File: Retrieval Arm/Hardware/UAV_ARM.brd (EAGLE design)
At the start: 100 x 80 mm, 20 parts, among them Q1 Q_ATMEGA328P, Q2 Q_LTC490, Q3 Q_LDO, X1 X_HC49SCRYSTAL

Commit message: Revised Board #4
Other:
- board size 100 x 80 mm -> 54.6 x 47 mm
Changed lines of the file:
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@@
 <setting verticaltext="up"/>
 </settings>
-<grid distance="0.05" unitdist="inch" unit="inch" style="lines" multiple="1" display="no" altdistance="0.025" altunitdist="inch" altunit="inch"/>
+<grid distance="0.05" unitdist="inch" unit="inch" style="lines" multiple="1" display="yes" altdistance="0.005" altunitdist="inch" altunit="inch"/>
 <layers>
 <layer number="1" name="Top" color="4" fill="1" visible="yes" active="yes"/>
@@
 <board>
 <plain>
-<wire x1="0" y1="0" x2="100" y2="0" width="0" layer="20"/>
-<wire x1="100" y1="0" x2="100" y2="80" width="0" layer="20"/>
-<wire x1="100" y1="80" x2="0" y2="80" width="0" layer="20"/>
-<wire x1="0" y1="80" x2="0" y2="0" width="0" layer="20"/>
-<hole x="3.81" y="34.29" drill="0.6"/>
-<hole x="53.34" y="34.29" drill="0.6"/>
-<hole x="53.34" y="77.47" drill="0.6"/>
-<hole x="20.32" y="77.47" drill="0.6"/>
+<wire x1="0" y1="80.01" x2="0" y2="33.02" width="0" layer="20"/>
+<wire x1="0" y1="33.02" x2="54.61" y2="33.02" width="0" layer="20"/>
+<wire x1="54.61" y1="33.02" x2="54.61" y2="80.01" width="0" layer="20"/>
+<wire x1="54.61" y1="80.01" x2="0" y2="80.01" width="0" layer="20"/>
 </plain>
 <attributes>

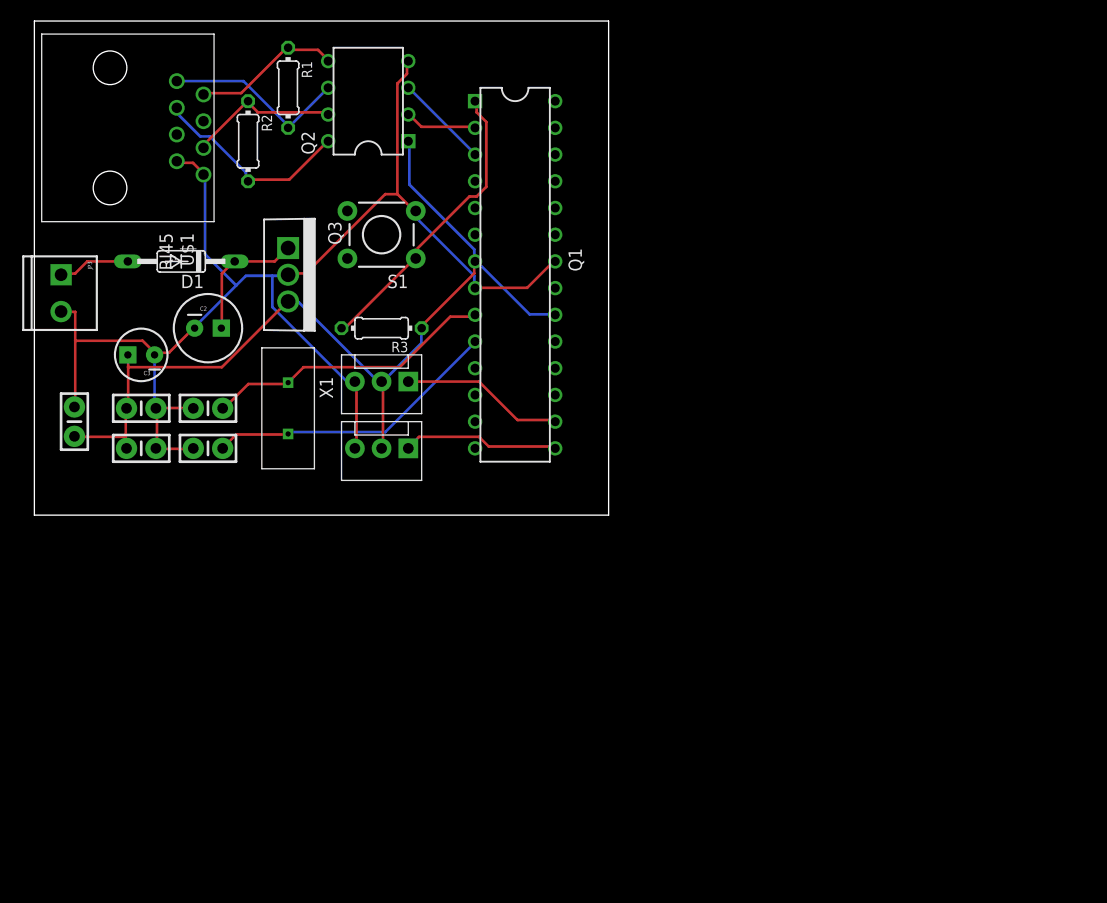
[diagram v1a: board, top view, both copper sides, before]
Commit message: Redesigned for new arm
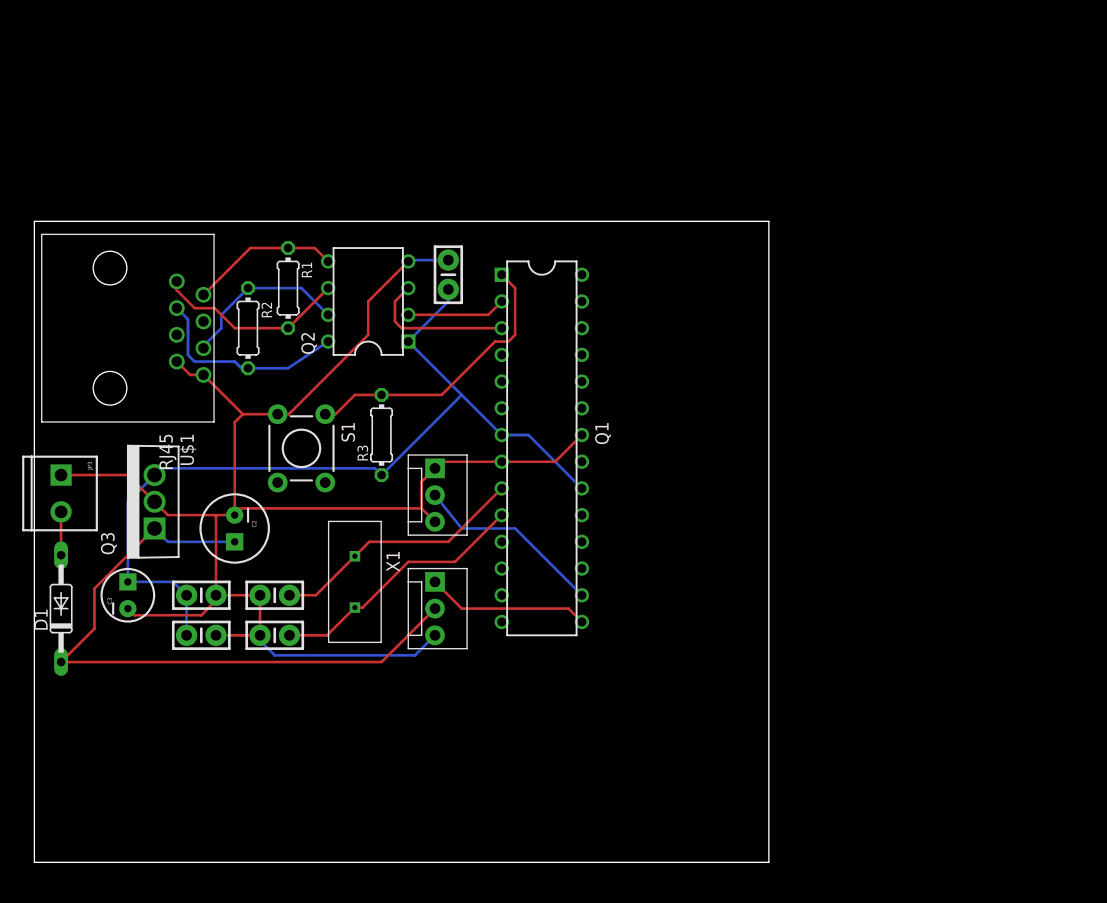
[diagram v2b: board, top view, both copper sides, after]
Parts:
- moved C1 38.2 mm to (39.4, 55.9)
- moved D1 34.9 mm to (2.54, 24.1), turned to 90 degrees
- moved Q3 25.0 mm to (11.4, 34.3), turned to 90 degrees
- moved C3 22.9 mm to (8.89, 25.4), turned to 90 degrees
- moved S1 21.7 mm to (25.4, 39.4), turned to 270 degrees
- moved C2 19.2 mm to (19.1, 31.8), turned to 270 degrees
- moved JP3 19.1 mm to (2.54, 36.8)
- moved Q2 19.0 mm to (31.8, 53.3)
- moved R1 19.0 mm to (24.1, 54.6)
- moved U$1 19.0 mm to (8.89, 50.8)
- moved C6 18.9 mm to (22.9, 25.4)
- moved C7 18.9 mm to (22.9, 21.6)
- moved C5 18.7 mm to (15.9, 25.4)
- moved C4 18.7 mm to (15.9, 21.6)
- moved R2 17.8 mm to (20.3, 50.8)
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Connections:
- removed net N$12: JP2.1, Q1.16
- removed net N$14 (its old number): C1.1, C3.1, C4.1, C5.1, JP1.2, JP2.2, Q1.20, Q1.7, Q2.1, Q3.3, R3.1
- new net N$15: D1.A, JP3.2
- new net N$6: C1.1, C3.1, C4.1, C5.1, Q1.20, Q1.7, Q2.1, Q3.3, R3.1
- net GND: now also JP2.1, JP3.1; no longer JP3.2
- net N$13: now also JP2.2, Q1.16; no longer D1.A, JP3.1
- net N$5: now also JP1.2
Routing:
- net N$14 (its old number): track 89.4 -> 0.00 mm
- net N$6: track 0.00 -> 82.9 mm
- net N$5: track 12.5 -> 62.2 mm
- net GND: track 133.5 -> 151.1 mm
- net N$12: track 15.5 -> 0.00 mm
- net N$13: track 6.83 -> 18.1 mm
- net N$7: track 8.99 -> 14.1 mm
- net N$15: track 0.00 -> 4.12 mm
- net N$11: track 28.3 -> 24.9 mm
- net N$10: track 27.7 -> 24.4 mm
- net N$8: track 6.88 -> 9.42 mm
- net N$2: track 14.6 -> 16.1 mm
- net N$9: track 28.4 -> 27.4 mm
- net N$14: track 14.9 -> 15.5 mm
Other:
- board size 54.6 x 47 mm -> 69.8 x 61 mm

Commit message: I am taking over electronics hardware development
The previous board was literally the worst PCB i’ve ever seen. EAGLE’s
autorouter should not be used under any circumstances. I can be quoted
on both of these statements, and will not apologize for either.

That being said, I redesigned the entire board using the 32u4 Breakout
board, proper SMT, proper layout, intelligent routing, PoRC Spec, and a
visually symmetrical design. The design should still be checked, as the
connections used are not necessarily correct.
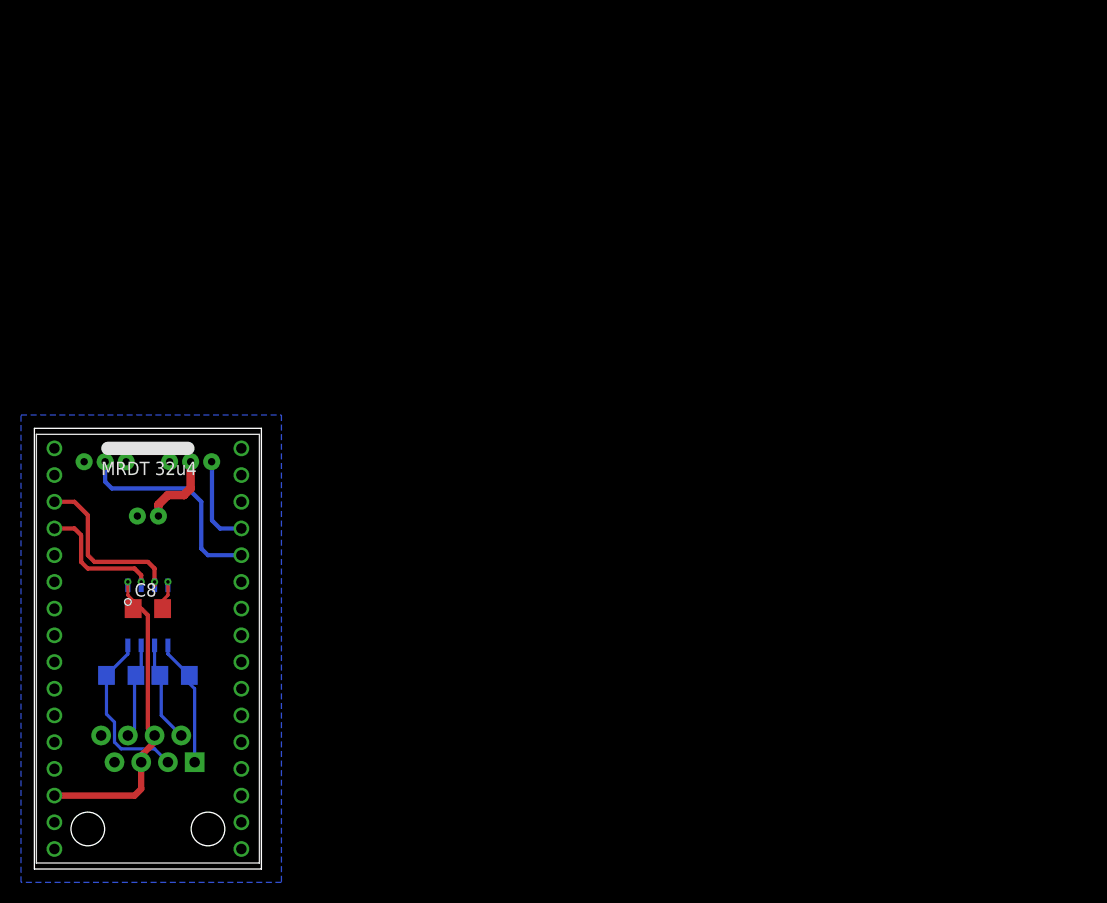
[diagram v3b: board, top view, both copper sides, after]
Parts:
- removed C1, C5: 1uF, SparkFun-Capacitors:CAP-PTH-SMALL-KIT
- removed C2: 100uF, SparkFun-Passives:CPOL-RADIAL-100UF-25V
- removed C3: 10uF, SparkFun-Passives:CPOL-RADIAL-10UF-25V
- removed C4: .01uF, SparkFun-Capacitors:CAP-PTH-SMALL-KIT
- removed C6, C7: 22pF, SparkFun-Capacitors:CAP-PTH-SMALL-KIT
- removed D1: 1N4446, diode:DO35-10
- removed Q1: Q_ATMEGA328P, MRDT-2014-All:DIP28
- removed Q2: Q_LTC490, MRDT-2014-All:DIP8
- removed Q3: Q_LDO, MRDT-2015-General:TO-220
- removed R1, R2: 120, resistor:0204/7
- removed R3: 10K, resistor:0204/7
- removed S1: SWITCH-MOMENTARY-2PTH, SparkFun-Electromechanical:TACTILE-PTH
- removed U$1: RJ45, MRDT-2014-All:RJ45-CAT5E
- removed X1: X_HC49SCRYSTAL, MRDT-2014-All:HC-49
- added C8: 1uF, resistor:C1206
- added R5, R6: 120 Ohm, SparkFun-Passives:1206
- added U$2: 32U4_BREAKOUT, MRDT-2015-General:32U4_MCU_DIP
- added U$3: MAX3077, MAX3077:MAX3070E
- added U$4: RJ45-8PTH, SparkFun-Connectors:RJ45-8
- JP1: value (none) -> M02JST-PTH-VERT; device SparkFun-Connectors:MOLEX-1X3 -> SparkFun-Connectors:JST-2-PTH-VERT
- JP2: device SparkFun-Connectors:MOLEX-1X3 -> SparkFun-Connectors:JST-3-PTH
- JP3: value M023.5MM -> (none); device SparkFun-Connectors:SCREWTERMINAL-3.5MM-2 -> SparkFun-Connectors:JST-3-PTH
- moved JP1 27.9 mm to (10.8, 32.4), flipped to the bottom, turned to 180 degrees
- moved JP2 23.2 mm to (14.9, 38.1), flipped to the bottom, turned to 0 degrees
- moved JP3 4.38 mm to (6.73, 38.1), flipped to the bottom, turned to 0 degrees
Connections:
- removed net N$10: C6.1, Q1.9, X1.P$1
- removed net N$11: C7.1, Q1.10, X1.P$2
- removed net N$13: JP2.2, Q1.16
- removed net N$14: JP1.1, Q1.15
- removed net N$15: D1.A, JP3.2
- removed net N$3: Q2.5, R1.1, U$1.2
- removed net N$4: Q2.6, R1.2, U$1.1
- removed net N$5: C2.1, D1.C, JP1.2, Q3.1
- removed net N$6: C1.1, C3.1, C4.1, C5.1, Q1.20, Q1.7, Q2.1, Q3.3, R3.1
- removed net N$7: Q1.3, Q2.3
- removed net N$8: Q1.2, Q2.2
- removed net N$9: Q1.1, R3.2, S1.1
- new net +5V: C8.1, U$2.14, U$3.VCC, U$4.4, U$4.5
- new net N$12: R6.2, U$3.Y, U$4.1
- new net N$18: R6.1, U$3.Z, U$4.2
- new net N$19: R5.2, U$3.B, U$4.6
- new net N$20: R5.1, U$3.A, U$4.3
- new net N$21: U$2.3, U$3.DI
- new net RXD: U$2.4, U$3.RO
- new net VIN: JP1.2, JP2.2
- net GND: now also C8.2, JP1.1, JP3.3, U$2.15, U$2.17, U$3.GND, U$4.7, U$4.8; no longer C1.2, C2.2, C3.2, C4.2, C5.2, C6.2, C7.2, JP1.3, JP2.1, Q1.22, Q1.8, Q2.4, Q3.2, S1.3, U$1.7, U$1.8
- net N$1: now also JP3.2, U$2.28; no longer Q2.8, R2.2, U$1.3
- net N$2: now also JP2.1, U$2.29; no longer Q2.7, R2.1, U$1.6
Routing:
- net GND: track 151.1 -> 2.75 mm, vias 0 -> 1
- net N$6: track 82.9 -> 0.00 mm
- net N$5: track 62.2 -> 0.00 mm
- net +5V: track 0.00 -> 30.5 mm, vias 0 -> 1
- net N$9: track 27.4 -> 0.00 mm
- net N$11: track 24.9 -> 0.00 mm
- net N$10: track 24.4 -> 0.00 mm
- net N$4: track 18.3 -> 0.00 mm
- net N$13: track 18.1 -> 0.00 mm
- net N$21: track 0.00 -> 16.3 mm, vias 0 -> 1
- net N$20: track 0.00 -> 16.2 mm
- net N$14: track 15.5 -> 0.00 mm
- net N$3: track 14.2 -> 0.00 mm
- net N$7: track 14.1 -> 0.00 mm
- net RXD: track 0.00 -> 12.9 mm, vias 0 -> 1
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- added copper zone on layer 16, net GND
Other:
- board size 69.8 x 61 mm -> 21.6 x 41.9 mm
